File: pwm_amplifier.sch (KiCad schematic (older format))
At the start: 8 parts, among them Q1 IRF540N, U3 PC817

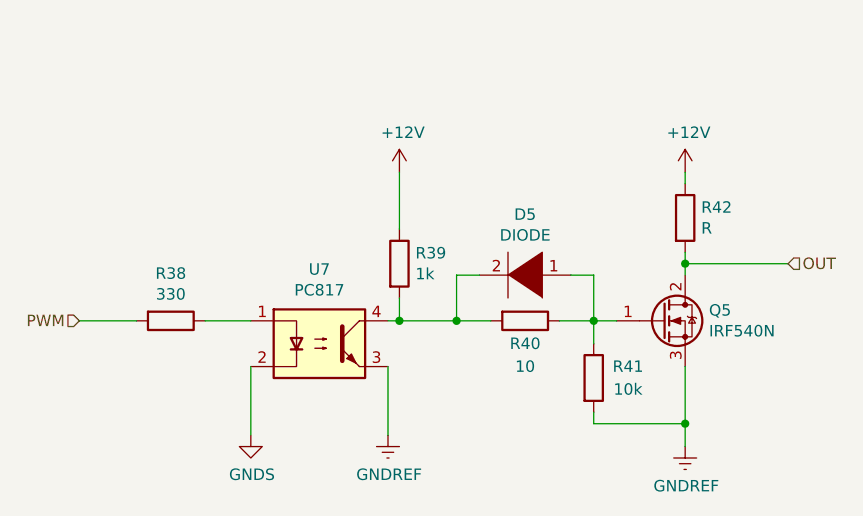
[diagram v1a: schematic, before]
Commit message: [layout] complete component place
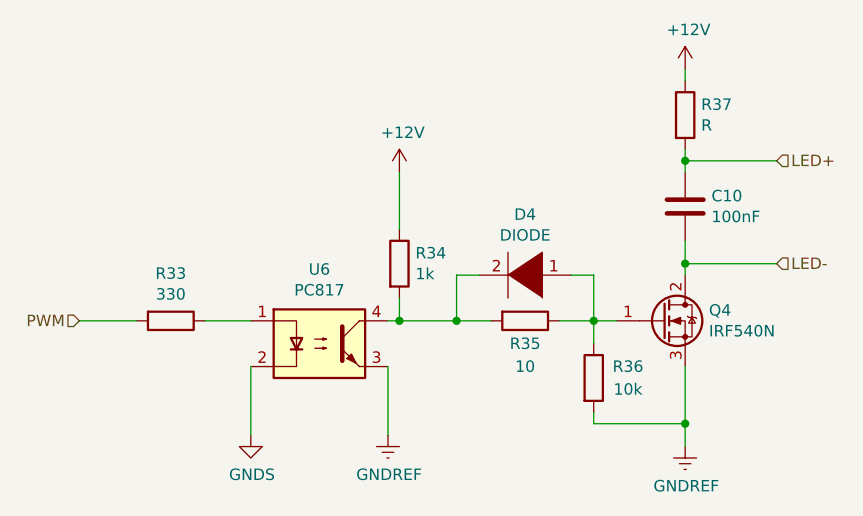
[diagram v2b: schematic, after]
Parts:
- added C7: 100nF, Capacitor_SMD:C_0603_1608Metric, symbol Device:C
- D1: footprint Diode_SMD:D_0603_1608Metric -> local_footprint:1N4007_SMD
- Q1: footprint Package_TO_SOT_THT:TO-220-3_Vertical -> local_footprint:TO-220_heatsink
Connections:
- net OUT renamed LED+
- net LED+: now also C7.1; no longer Q1.2 (D)
- new net LED-: C7.2, Q1.2 (D)
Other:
- moved on the sheet: R37

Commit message: [layout] complete 90%
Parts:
- renumbered R18 to R20, R19 to R21, R20 to R22, R21 to R23, R22 to R24

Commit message: [layout] completed
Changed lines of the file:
@@
 AR Path="/6152A6A8/61745C6B" Ref="U6"  Part="1"
 AR Path="/6152E7D4/61745C6B" Ref="U7"  Part="1"
-F 0 "U4" H 4750 3875 50  0000 C CNN
+F 0 "U7" H 4750 3875 50  0000 C CNN
 F 1 "PC817" H 4750 3784 50  0000 C CNN
 F 2 "Package_DIP:DIP-4_W7.62mm" H 4550 3350 50  0001 L CIN
@@
 AR Path="/6152A6A8/61745C71" Ref="Q4"  Part="1"
 AR Path="/6152E7D4/61745C71" Ref="Q5"  Part="1"
-F 0 "Q2" H 6454 3496 50  0000 L CNN
+F 0 "Q5" H 6454 3496 50  0000 L CNN
 F 1 "IRF540N" H 6454 3405 50  0000 L CNN
 F 2 "local_footprint:TO-220_heatsink" H 6500 3375 50  0001 L CIN
@@
 AR Path="/6152A6A8/61747C76" Ref="R35"  Part="1"
 AR Path="/6152E7D4/61747C76" Ref="R40"  Part="1"
-F 0 "R25" V 3893 3450 50  0000 C CNN
+F 0 "R40" V 3893 3450 50  0000 C CNN
 F 1 "330" V 3984 3450 50  0000 C CNN
 F 2 "Resistor_SMD:R_0603_1608Metric" V 4030 3450 50  0001 C CNN
@@
 AR Path="/6152A6A8/61748253" Ref="R36"  Part="1"
 AR Path="/6152E7D4/61748253" Ref="R41"  Part="1"
-F 0 "R26" H 5170 3246 50  0000 L CNN
+F 0 "R41" H 5170 3246 50  0000 L CNN
 F 1 "1k" H 5170 3155 50  0000 L CNN
 F 2 "Resistor_SMD:R_0603_1608Metric" V 5030 3200 50  0001 C CNN
@@
 AR Path="/6152A6A8/61748F7D" Ref="D4"  Part="1"
 AR Path="/6152E7D4/61748F7D" Ref="D5"  Part="1"
-F 0 "D2" H 5650 2985 50  0000 C CNN
+F 0 "D5" H 5650 2985 50  0000 C CNN
 F 1 "DIODE" H 5650 3076 50  0000 C CNN
 F 2 "local_footprint:1N4007_SMD" H 5650 3250 50  0001 C CNN
@@
 AR Path="/6152A6A8/6175B05A" Ref="R37"  Part="1"
 AR Path="/6152E7D4/6175B05A" Ref="R42"  Part="1"
-F 0 "R27" V 5750 3450 50  0000 C CNN
+F 0 "R42" V 5750 3450 50  0000 C CNN
 F 1 "10" V 5850 3450 50  0000 C CNN
 F 2 "Resistor_SMD:R_0603_1608Metric" V 5580 3450 50  0001 C CNN
@@
 AR Path="/6152A6A8/6175E102" Ref="R38"  Part="1"
 AR Path="/6152E7D4/6175E102" Ref="R43"  Part="1"
-F 0 "R28" H 6100 3750 50  0000 C CNN
+F 0 "R43" H 6100 3750 50  0000 C CNN
 F 1 "10k" H 6100 3650 50  0000 C CNN
 F 2 "Resistor_THT:R_Axial_DIN0207_L6.3mm_D2.5mm_P7.62mm_Horizontal" V 5880 3700 50  0001 C CNN
@@
 AR Path="/6152A6A8/61528FF9" Ref="#PWR045"  Part="1"
 AR Path="/6152E7D4/61528FF9" Ref="#PWR050"  Part="1"
-F 0 "#PWR035" H 4450 3700 50  0001 C CNN
+F 0 "#PWR050" H 4450 3700 50  0001 C CNN
 F 1 "GNDS" H 4455 3777 50  0000 C CNN
 F 2 "" H 4450 3950 50  0001 C CNN
@@
 AR Path="/6152A6A8/61528FFF" Ref="#PWR049"  Part="1"
 AR Path="/6152E7D4/61528FFF" Ref="#PWR054"  Part="1"
-F 0 "#PWR039" H 6350 3750 50  0001 C CNN
+F 0 "#PWR054" H 6350 3750 50  0001 C CNN
 F 1 "GNDREF" H 6355 3827 50  0000 C CNN
 F 2 "" H 6350 4000 50  0001 C CNN
@@
 AR Path="/6152A6A8/6152B5BF" Ref="#PWR046"  Part="1"
 AR Path="/6152E7D4/6152B5BF" Ref="#PWR051"  Part="1"
-F 0 "#PWR036" H 5050 3700 50  0001 C CNN
+F 0 "#PWR051" H 5050 3700 50  0001 C CNN
 F 1 "GNDREF" H 5055 3777 50  0000 C CNN
 F 2 "" H 5050 3950 50  0001 C CNN
@@
 AR Path="/6152A6A8/6152A763" Ref="R39"  Part="1"
 AR Path="/6152E7D4/6152A763" Ref="R44"  Part="1"
-F 0 "R29" H 6420 2596 50  0000 L CNN
+F 0 "R44" H 6420 2596 50  0000 L CNN
 F 1 "R" H 6420 2505 50  0000 L CNN
 F 2 "Resistor_SMD:R_0603_1608Metric" V 6280 2550 50  0001 C CNN
@@
 AR Path="/6152A6A8/61602D7C" Ref="#PWR048"  Part="1"
 AR Path="/6152E7D4/61602D7C" Ref="#PWR053"  Part="1"
-F 0 "#PWR038" H 6350 2200 50  0001 C CNN
+F 0 "#PWR053" H 6350 2200 50  0001 C CNN
 F 1 "+12V" H 6365 2523 50  0000 C CNN
 F 2 "" H 6350 2350 50  0001 C CNN
@@
 AR Path="/6152A6A8/616034CD" Ref="#PWR047"  Part="1"
 AR Path="/6152E7D4/616034CD" Ref="#PWR052"  Part="1"
-F 0 "#PWR037" H 5100 2650 50  0001 C CNN
+F 0 "#PWR052" H 5100 2650 50  0001 C CNN
 F 1 "+12V" H 5115 2973 50  0000 C CNN
 F 2 "" H 5100 2800 50  0001 C CNN
@@
 AR Path="/6152A6A8/6150FD88" Ref="C10"  Part="1"
 AR Path="/6152E7D4/6150FD88" Ref="C11"  Part="1"
-F 0 "C8" H 6465 2996 50  0000 L CNN
+F 0 "C11" H 6465 2996 50  0000 L CNN
 F 1 "100nF" H 6465 2905 50  0000 L CNN
 F 2 "Capacitor_SMD:C_0603_1608Metric" H 6388 2800 50  0001 C CNN

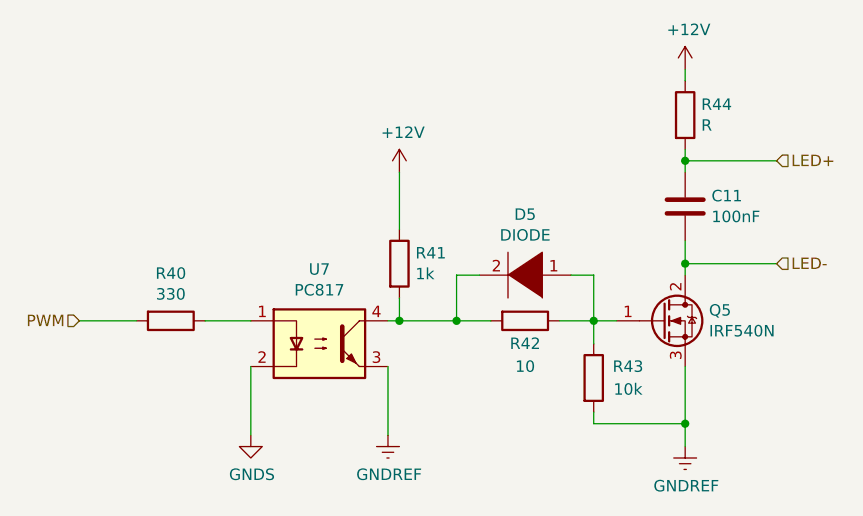
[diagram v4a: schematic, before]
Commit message: [layout] modify MountingHole size and footprint
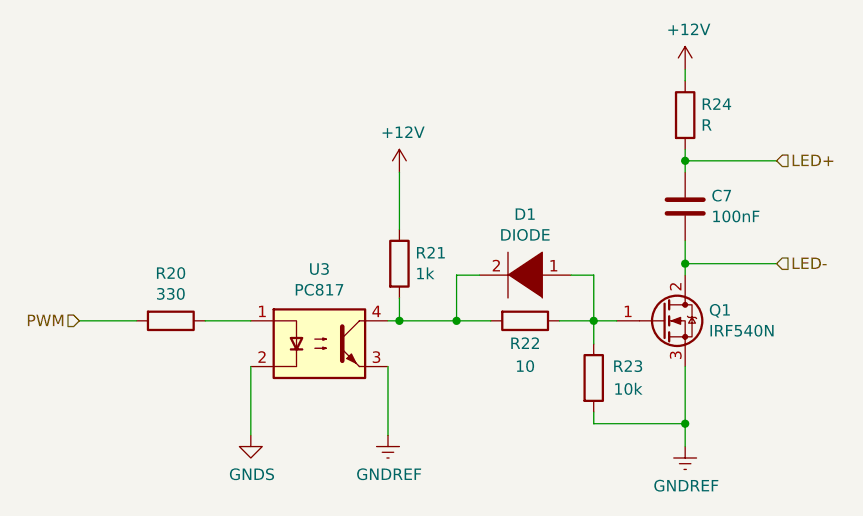
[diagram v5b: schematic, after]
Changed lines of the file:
@@
 $Descr A4 11693 8268
 encoding utf-8
-Sheet 3 6
+Sheet 2 6
 Title ""
 Date ""
@@
 AR Path="/6152A6A8/61745C6B" Ref="U6"  Part="1"
 AR Path="/6152E7D4/61745C6B" Ref="U7"  Part="1"
-F 0 "U7" H 4750 3875 50  0000 C CNN
+F 0 "U3" H 4750 3875 50  0000 C CNN
 F 1 "PC817" H 4750 3784 50  0000 C CNN
 F 2 "Package_DIP:DIP-4_W7.62mm" H 4550 3350 50  0001 L CIN
@@
 AR Path="/6152A6A8/61745C71" Ref="Q4"  Part="1"
 AR Path="/6152E7D4/61745C71" Ref="Q5"  Part="1"
-F 0 "Q5" H 6454 3496 50  0000 L CNN
+F 0 "Q1" H 6454 3496 50  0000 L CNN
 F 1 "IRF540N" H 6454 3405 50  0000 L CNN
 F 2 "local_footprint:TO-220_heatsink" H 6500 3375 50  0001 L CIN
@@
 AR Path="/6152A6A8/61747C76" Ref="R35"  Part="1"
 AR Path="/6152E7D4/61747C76" Ref="R40"  Part="1"
-F 0 "R40" V 3893 3450 50  0000 C CNN
+F 0 "R20" V 3893 3450 50  0000 C CNN
 F 1 "330" V 3984 3450 50  0000 C CNN
 F 2 "Resistor_SMD:R_0603_1608Metric" V 4030 3450 50  0001 C CNN
@@
 AR Path="/6152A6A8/61748253" Ref="R36"  Part="1"
 AR Path="/6152E7D4/61748253" Ref="R41"  Part="1"
-F 0 "R41" H 5170 3246 50  0000 L CNN
+F 0 "R21" H 5170 3246 50  0000 L CNN
 F 1 "1k" H 5170 3155 50  0000 L CNN
 F 2 "Resistor_SMD:R_0603_1608Metric" V 5030 3200 50  0001 C CNN
@@
 AR Path="/6152A6A8/61748F7D" Ref="D4"  Part="1"
 AR Path="/6152E7D4/61748F7D" Ref="D5"  Part="1"
-F 0 "D5" H 5650 2985 50  0000 C CNN
+F 0 "D1" H 5650 2985 50  0000 C CNN
 F 1 "DIODE" H 5650 3076 50  0000 C CNN
 F 2 "local_footprint:1N4007_SMD" H 5650 3250 50  0001 C CNN
@@
 AR Path="/6152A6A8/6175B05A" Ref="R37"  Part="1"
 AR Path="/6152E7D4/6175B05A" Ref="R42"  Part="1"
-F 0 "R42" V 5750 3450 50  0000 C CNN
+F 0 "R22" V 5750 3450 50  0000 C CNN
 F 1 "10" V 5850 3450 50  0000 C CNN
 F 2 "Resistor_SMD:R_0603_1608Metric" V 5580 3450 50  0001 C CNN
@@
 AR Path="/6152A6A8/6175E102" Ref="R38"  Part="1"
 AR Path="/6152E7D4/6175E102" Ref="R43"  Part="1"
-F 0 "R43" H 6100 3750 50  0000 C CNN
+F 0 "R23" H 6100 3750 50  0000 C CNN
 F 1 "10k" H 6100 3650 50  0000 C CNN
 F 2 "Resistor_THT:R_Axial_DIN0207_L6.3mm_D2.5mm_P7.62mm_Horizontal" V 5880 3700 50  0001 C CNN
@@
 AR Path="/6152A6A8/6152A763" Ref="R39"  Part="1"
 AR Path="/6152E7D4/6152A763" Ref="R44"  Part="1"
-F 0 "R44" H 6420 2596 50  0000 L CNN
+F 0 "R24" H 6420 2596 50  0000 L CNN
 F 1 "R" H 6420 2505 50  0000 L CNN
 F 2 "Resistor_SMD:R_0603_1608Metric" V 6280 2550 50  0001 C CNN
@@
 AR Path="/6152A6A8/6150FD88" Ref="C10"  Part="1"
 AR Path="/6152E7D4/6150FD88" Ref="C11"  Part="1"
-F 0 "C11" H 6465 2996 50  0000 L CNN
+F 0 "C7" H 6465 2996 50  0000 L CNN
 F 1 "100nF" H 6465 2905 50  0000 L CNN
 F 2 "Capacitor_SMD:C_0603_1608Metric" H 6388 2800 50  0001 C CNN
